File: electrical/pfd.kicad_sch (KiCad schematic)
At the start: 8 parts

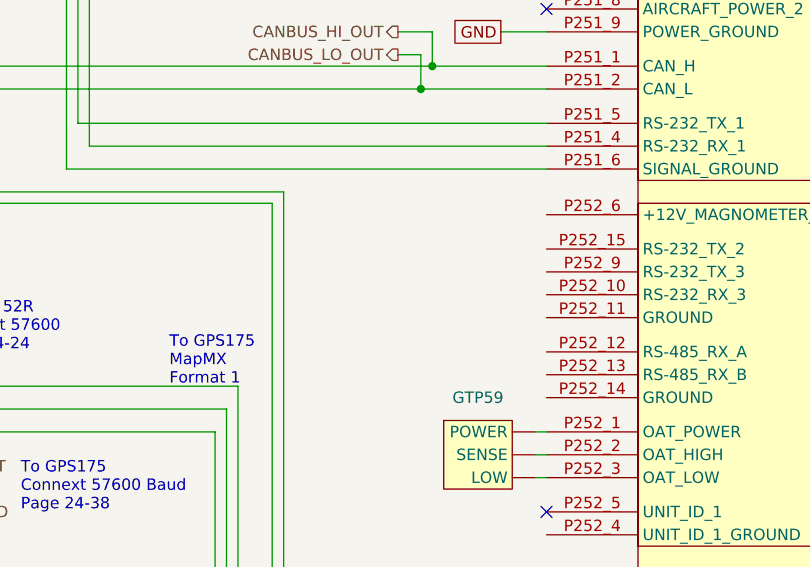
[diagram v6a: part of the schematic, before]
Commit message: Added Altitude Encoder for 320, also added RS232 air data to Transponder in case upgrade to a GTX 327
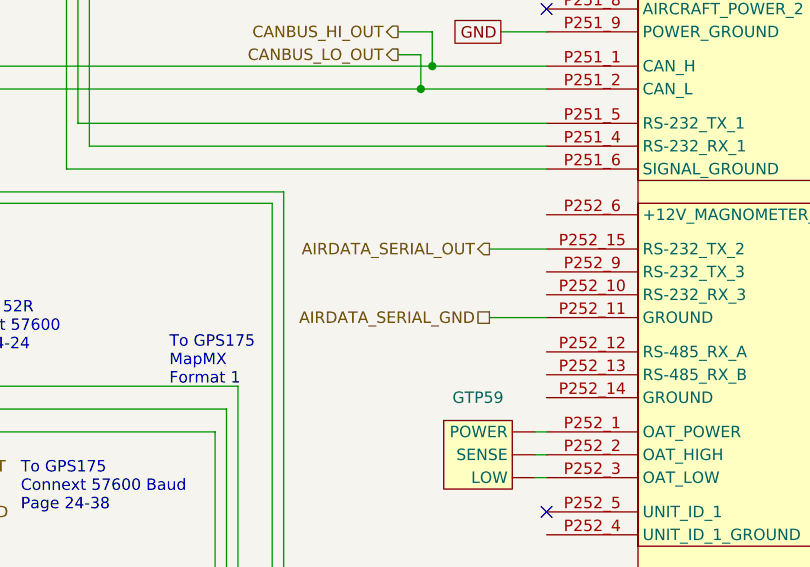
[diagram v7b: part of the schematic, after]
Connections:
- net AIRDATA_SERIAL_GND: now reaches GSU25.P252_11 (GROUND)
- net AIRDATA_SERIAL_OUT: now reaches GSU25.P252_15 (RS-232_TX_2)
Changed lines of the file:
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@@
     (title "PFD & ADAHRS")
     (date "2024-05-07")
-    (rev "1.0")
+    (rev "1.0.2")
     (company "N877RV")
   )
@@
     (stroke (width 0) (type default))
   )
+  (wire (pts (xy 148.59 80.01) (xy 154.94 80.01))
+    (stroke (width 0) (type default))
+  )
   (wire (pts (xy 85.09 62.23) (xy 140.97 62.23))
     (stroke (width 0) (type default))
@@
   )
   (wire (pts (xy 119.38 129.54) (xy 161.29 129.54))
+    (stroke (width 0) (type default))
+  )
+  (wire (pts (xy 148.59 87.63) (xy 154.94 87.63))
     (stroke (width 0) (type default))
   )
@@
     (effects (font (size 1.27 1.27)) (justify left))
   )
+  (hierarchical_label "AIRDATA_SERIAL_GND" (shape passive) (at 148.59 87.63 180) (fields_autoplaced)
+    (effects (font (size 1.27 1.27)) (justify right))
+  )
   (hierarchical_label "EIS_SERIAL_IN" (shape input) (at 68.58 115.57 0) (fields_autoplaced)
     (effects (font (size 1.27 1.27)) (justify left))
@@
     (effects (font (size 1.27 1.27)) (justify right))
   )
+  (hierarchical_label "AIRDATA_SERIAL_OUT" (shape output) (at 148.59 80.01 180) (fields_autoplaced)
+    (effects (font (size 1.27 1.27)) (justify right))
+  )
